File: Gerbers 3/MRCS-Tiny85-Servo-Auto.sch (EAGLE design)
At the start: 15 parts, among them U1 ATTINY85-20PU

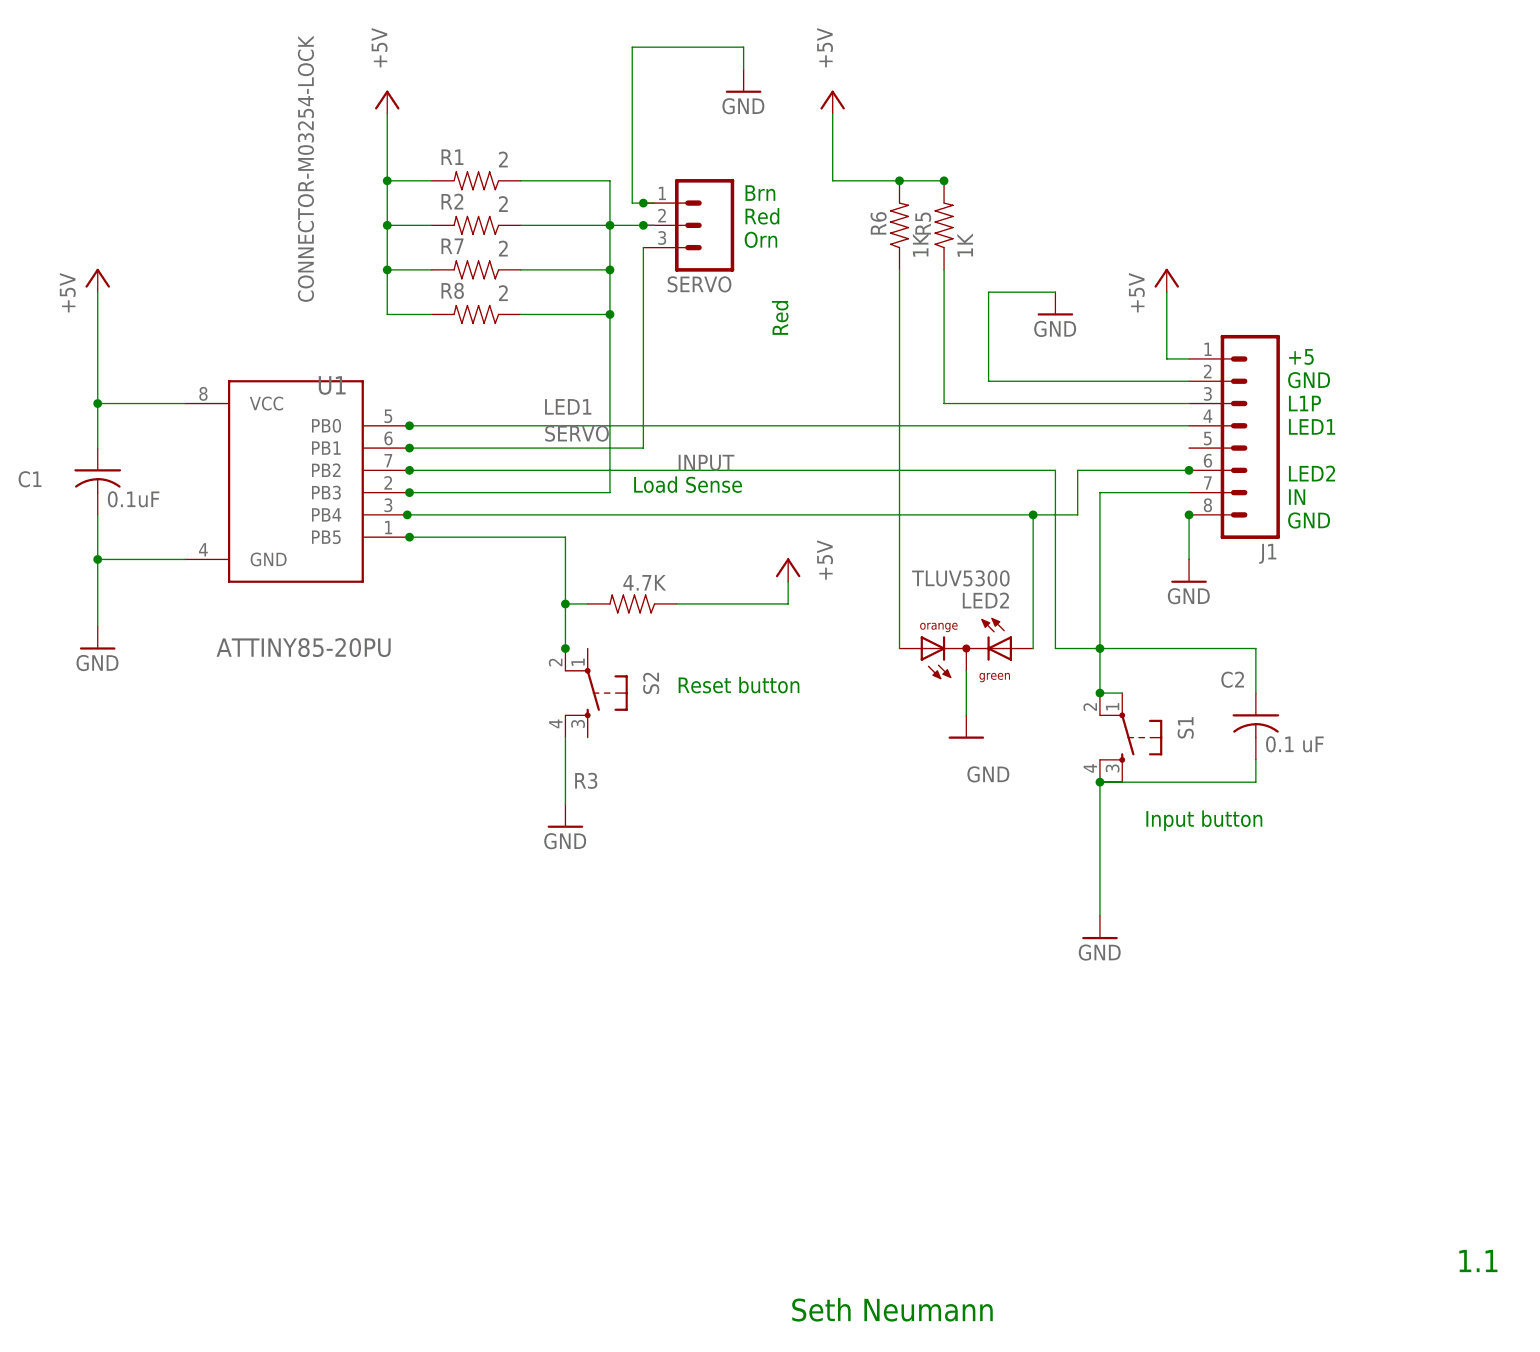
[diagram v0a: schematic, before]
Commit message: Moved one of the push buttons away from socket
This makes it easier to remove the ATTiny for reprogramming
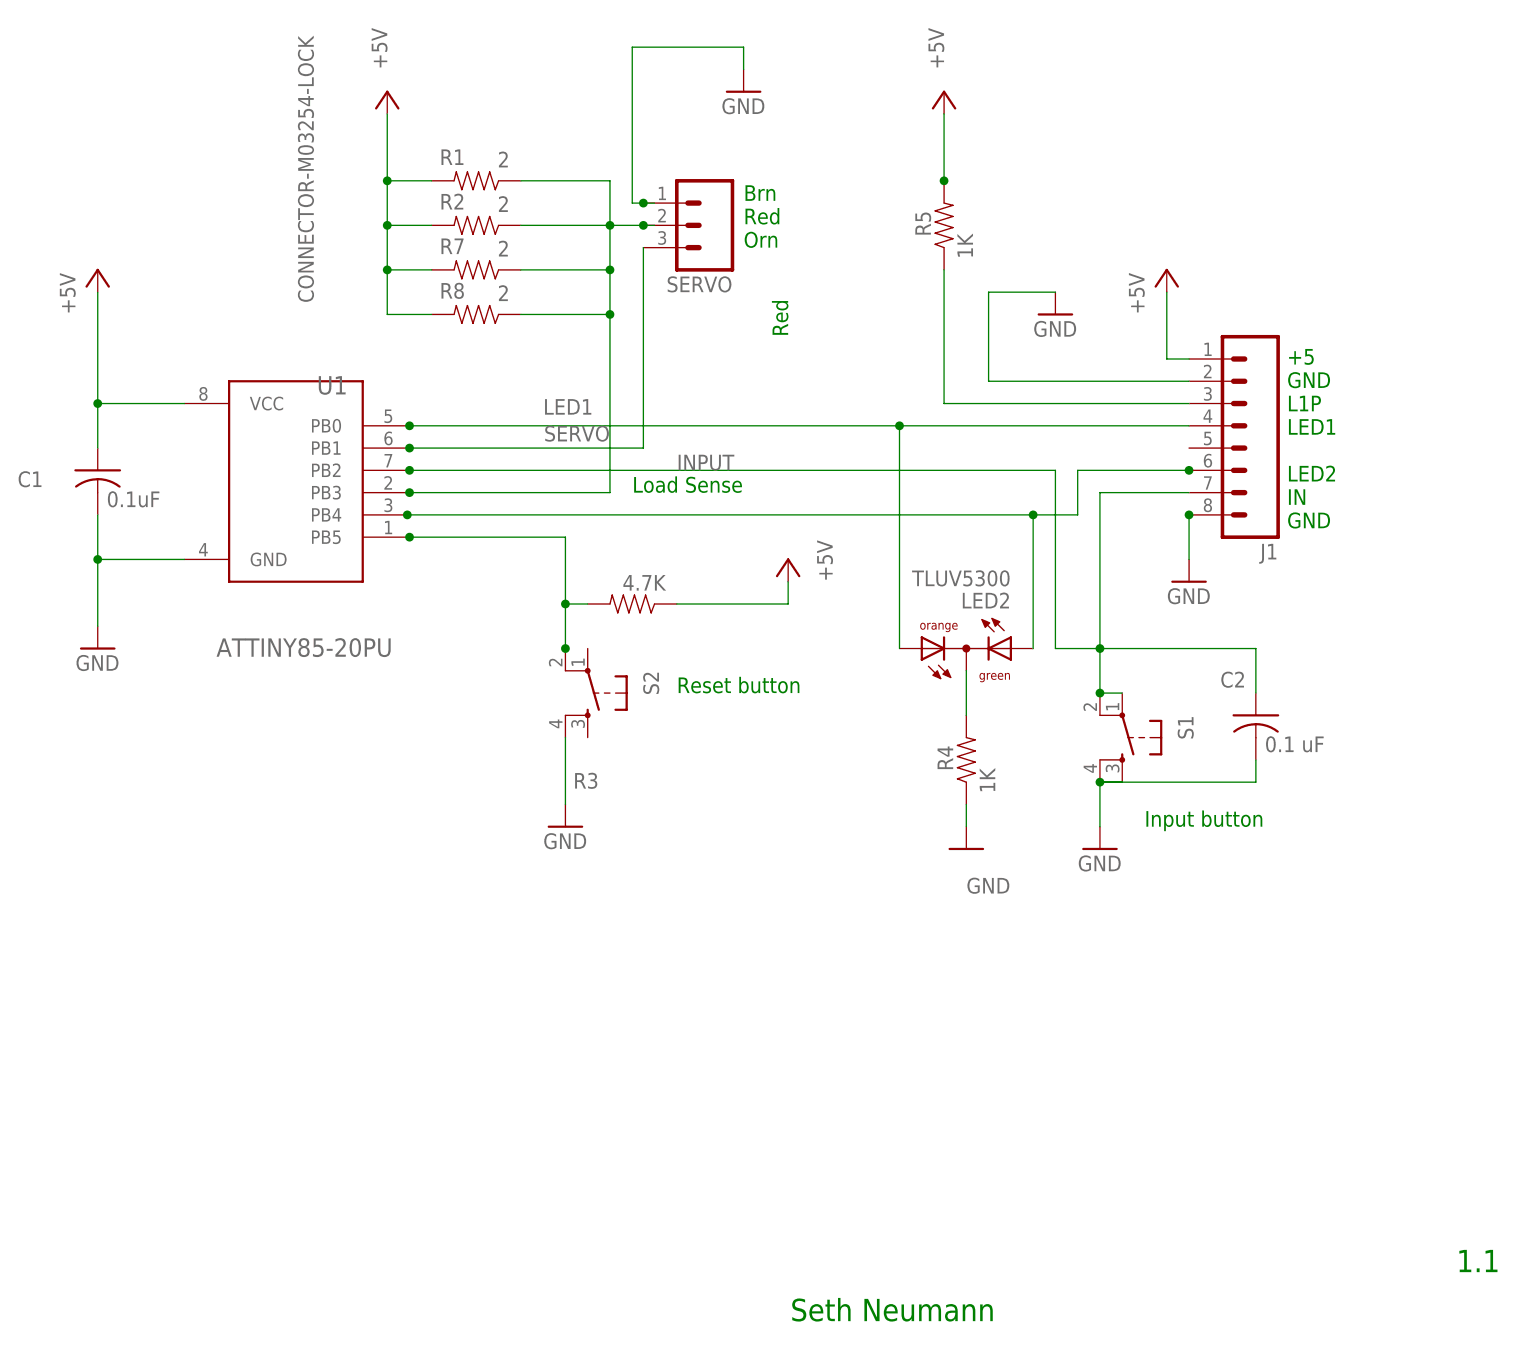
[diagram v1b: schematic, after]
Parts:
- removed R6: 1K, SPCoast:RPTH04
- added R4: 1K, SPCoast:RPTH04
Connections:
- removed net LED2PWR: LED2.AO, R6.1
- new net N$1: LED2.CC, R4.2
- net +5V: no longer R6.2
- net GND: now also R4.1; no longer LED2.CC
- net LED1: now also LED2.AO
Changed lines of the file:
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@@
 <part name="S2" library="SparkFun-Electromechanical" deviceset="TAC_SWITCH" device="PTH"/>
 <part name="GND6" library="SPCoast" deviceset="GND" device=""/>
-<part name="R6" library="SPCoast" deviceset="R*" device="PTH04" value="1K"/>
 <part name="R7" library="SPCoast" deviceset="R*" device="PTH04" value="2"/>
 <part name="R8" library="SPCoast" deviceset="R*" device="PTH04" value="2"/>
 <part name="LED2" library="led" deviceset="TLUV5300" device=""/>
 <part name="GND7" library="SPCoast" deviceset="GND" device=""/>
+<part name="R4" library="SPCoast" deviceset="R*" device="PTH04" value="1K"/>
 </parts>
 <sheets>
@@
 <attribute name="VALUE" x="198.882" y="153.67" size="1.778" layer="96" rot="R90"/>
 </instance>
-<instance part="GND2" gate="1" x="213.36" y="76.2" smashed="yes">
-<attribute name="VALUE" x="210.82" y="73.66" size="1.778" layer="96"/>
+<instance part="GND2" gate="1" x="213.36" y="86.36" smashed="yes">
+<attribute name="VALUE" x="210.82" y="83.82" size="1.778" layer="96"/>
 </instance>
 <instance part="P+4" gate="1" x="132.08" y="172.72" smashed="yes">
@@
 <attribute name="VALUE" x="218.44" y="147.32" size="1.778" layer="96" rot="R90"/>
 </instance>
-<instance part="P+6" gate="1" x="182.88" y="172.72" smashed="yes">
-<attribute name="VALUE" x="182.88" y="175.26" size="1.778" layer="96" rot="R90"/>
+<instance part="P+6" gate="1" x="195.58" y="172.72" smashed="yes">
+<attribute name="VALUE" x="195.58" y="175.26" size="1.778" layer="96" rot="R90"/>
 </instance>
 <instance part="SERVO" gate="G$1" x="167.64" y="157.48" smashed="yes" rot="R180">
@@
 <attribute name="VALUE" x="149.86" y="86.36" size="1.778" layer="96"/>
 </instance>
-<instance part="R6" gate="R" x="190.5" y="157.48" smashed="yes" rot="R90">
-<attribute name="NAME" x="189.0014" y="156.21" size="1.778" layer="95" rot="R90"/>
-<attribute name="VALUE" x="193.802" y="153.67" size="1.778" layer="96" rot="R90"/>
-</instance>
 <instance part="R7" gate="R" x="142.24" y="152.4" smashed="yes" rot="R180">
 <attribute name="NAME" x="140.97" y="155.9814" size="1.778" layer="95" rot="R180"/>
@@
 </instance>
 <instance part="LED2" gate="G$1" x="198.12" y="109.22" rot="R90"/>
-<instance part="GND7" gate="1" x="198.12" y="99.06" smashed="yes">
-<attribute name="VALUE" x="198.12" y="93.98" size="1.778" layer="96"/>
+<instance part="GND7" gate="1" x="198.12" y="86.36" smashed="yes">
+<attribute name="VALUE" x="198.12" y="81.28" size="1.778" layer="96"/>
+</instance>
+<instance part="R4" gate="R" x="198.12" y="96.52" smashed="yes" rot="R90">
+<attribute name="NAME" x="196.6214" y="95.25" size="1.778" layer="95" rot="R90"/>
+<attribute name="VALUE" x="201.422" y="92.71" size="1.778" layer="96" rot="R90"/>
 </instance>
 </instances>
@@
 <segment>
 <pinref part="P+6" gate="1" pin="+5V"/>
-<wire x1="182.88" y1="170.18" x2="182.88" y2="162.56" width="0.4064" layer="91"/>
-<pinref part="R6" gate="R" pin="2"/>
-<wire x1="182.88" y1="162.56" x2="190.5" y2="162.56" width="0.4064" layer="91"/>
+<wire x1="195.58" y1="170.18" x2="195.58" y2="162.56" width="0.4064" layer="91"/>
 <pinref part="R5" gate="R" pin="2"/>
-<wire x1="190.5" y1="162.56" x2="195.58" y2="162.56" width="0.4064" layer="91"/>
-<junction x="190.5" y="162.56"/>
 <junction x="195.58" y="162.56"/>
 </segment>
@@
 <segment>
 <pinref part="GND2" gate="1" pin="GND"/>
-<wire x1="213.36" y1="93.98" x2="213.36" y2="78.74" width="0.4064" layer="91"/>
+<wire x1="213.36" y1="93.98" x2="213.36" y2="88.9" width="0.4064" layer="91"/>
 <pinref part="S1" gate="S" pin="4"/>
 <pinref part="S1" gate="S" pin="3"/>
@@
 </segment>
 <segment>
-<pinref part="LED2" gate="G$1" pin="CC"/>
+<pinref part="R4" gate="R" pin="1"/>
 <pinref part="GND7" gate="1" pin="GND"/>
-<wire x1="198.12" y1="106.68" x2="198.12" y2="101.6" width="0.4064" layer="91"/>
+<wire x1="198.12" y1="91.44" x2="198.12" y2="88.9" width="0.3048" layer="91"/>
 </segment>
 </net>
@@
 <wire x1="134.366" y1="134.62" x2="134.62" y2="134.62" width="0.3048" layer="91"/>
 <label x="149.86" y="135.89" size="1.778" layer="95"/>
-<wire x1="134.62" y1="134.62" x2="223.52" y2="134.62" width="0.3048" layer="91"/>
+<wire x1="134.62" y1="134.62" x2="190.5" y2="134.62" width="0.3048" layer="91"/>
 <junction x="134.62" y="134.62"/>
+<pinref part="LED2" gate="G$1" pin="AO"/>
+<wire x1="190.5" y1="134.62" x2="223.52" y2="134.62" width="0.3048" layer="91"/>
+<wire x1="190.5" y1="109.22" x2="190.5" y2="134.62" width="0.3048" layer="91"/>
+<junction x="190.5" y="134.62"/>
 </segment>
 </net>
@@
 <junction x="152.4" y="109.22"/>
 <junction x="134.62" y="121.92"/>
-</segment>
-</net>
-<net name="LED2PWR" class="0">
-<segment>
-<pinref part="R6" gate="R" pin="1"/>
-<pinref part="LED2" gate="G$1" pin="AO"/>
-<wire x1="190.5" y1="152.4" x2="190.5" y2="109.22" width="0.3048" layer="91"/>
 </segment>
 </net>
@@
 </segment>
 </net>
+<net name="N$1" class="0">
+<segment>
+<pinref part="LED2" gate="G$1" pin="CC"/>
+<pinref part="R4" gate="R" pin="2"/>
+<wire x1="198.12" y1="106.68" x2="198.12" y2="101.6" width="0.3048" layer="91"/>
+</segment>
+</net>
